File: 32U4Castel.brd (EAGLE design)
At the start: 27.9 x 22.9 mm, 19 parts, among them U1 ATMEGA32U4, Y1 16MHz

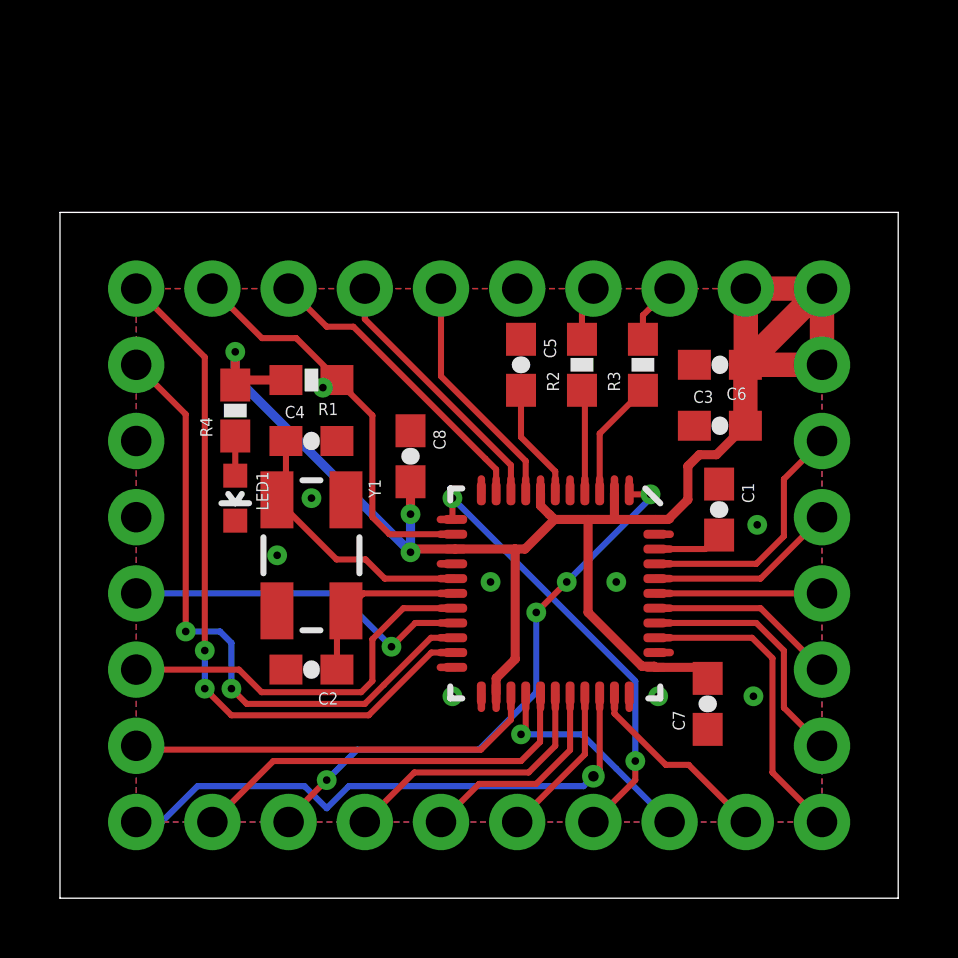
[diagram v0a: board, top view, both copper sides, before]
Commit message: Added pad, complete re-route
Fabrication was difficult because of non-ground vias where 32U4 wanted a pad. Added pad, rerouted everything. Improved silkscreen.
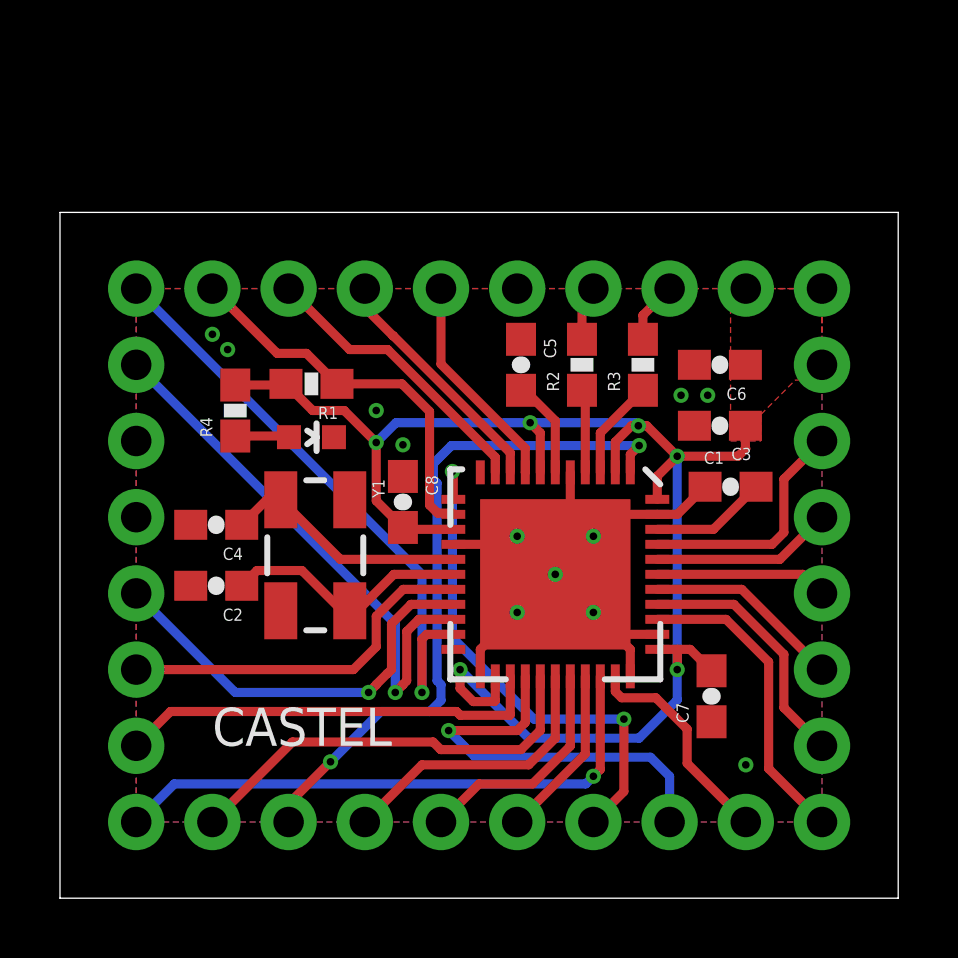
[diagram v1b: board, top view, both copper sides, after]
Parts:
- U1: device Testing:QFN-44-NOPAD_1:1-OUTFAKES -> 32U4Castel:TESTING_QFN-44
- moved C2 4.23 mm to (5.21, 10.4)
- moved C4 4.23 mm to (5.21, 12.4), turned to 180 degrees
- moved LED1 3.25 mm to (8.38, 15.4), turned to 270 degrees
- moved C8 1.55 mm to (11.4, 13.2)
- moved C1 0.85 mm to (22.4, 13.7), turned to 0 degrees
- moved U1 0.63 mm to (16.5, 10.8)
- moved C7 0.28 mm to (21.7, 6.73)
- moved Y1 0.13 mm to (8.51, 11.4)
- moved R1 0.13 mm to (8.38, 17.1)
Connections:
- net GND: now also U1.THERM
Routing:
- net GND: track 0.00 -> 26.7 mm, vias 9 -> 12
- net VCC: track 58.6 -> 52.4 mm, vias 3 -> 6
- net D12: track 7.59 -> 13.7 mm
- net D7: track 19.0 -> 23.2 mm, vias 4 -> 2
- net TXO: track 23.9 -> 20.3 mm, vias 2 -> 1
- net RXI: track 21.4 -> 18.4 mm, vias 2 -> 1
- net D11: track 14.6 -> 17.2 mm
- net N$2: track 5.97 -> 8.32 mm
- net D2: track 11.7 -> 14.1 mm
- net AREF: track 2.32 -> 3.88 mm
- net N$1: track 9.11 -> 8.22 mm
- net D13: track 6.54 -> 7.33 mm
- net D-: track 4.03 -> 3.32 mm
- net MISO: track 7.99 -> 7.29 mm
- net SCK: track 8.84 -> 8.14 mm
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- added copper zone on layer 1, net VCC
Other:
- board text added: "CASTEL"

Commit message: Updated 32U4Castel
Fixed mis-mapped SS pin and improved grounding.
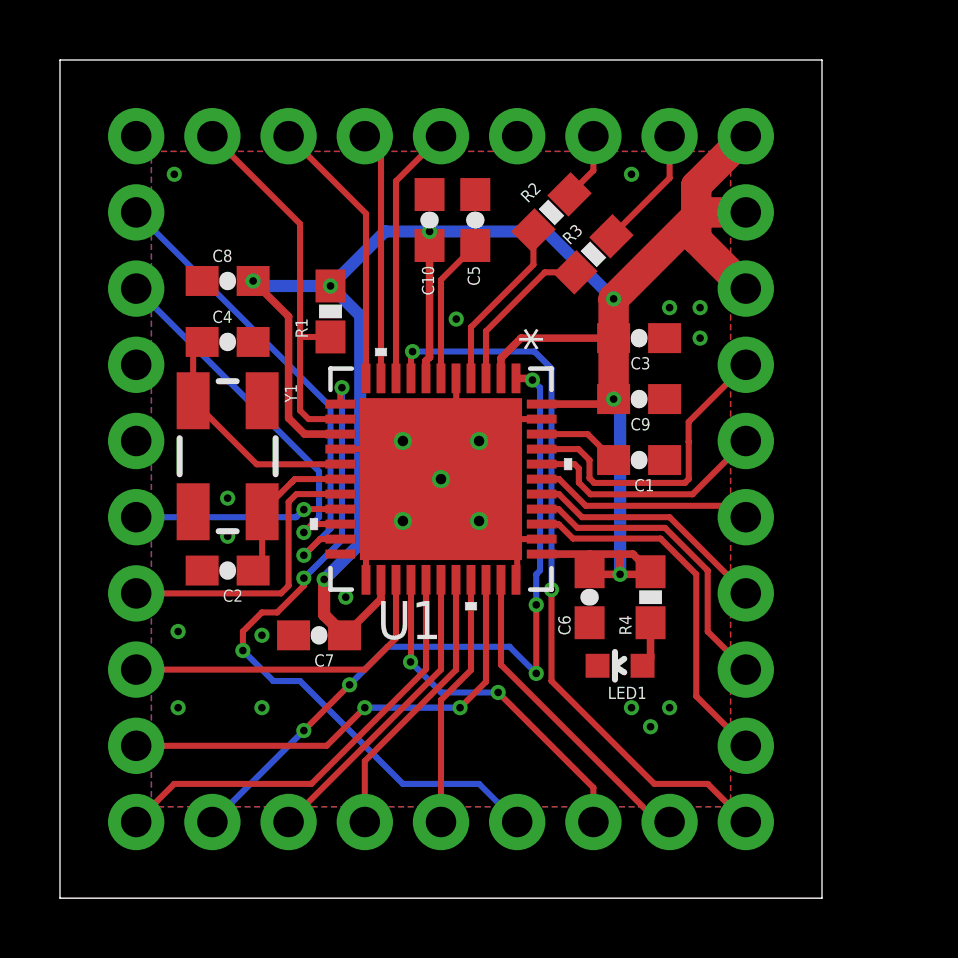
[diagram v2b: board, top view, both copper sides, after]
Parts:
- added C10, C9: 1uF, SparkFun:0603-CAP
- J1, J3: device SparkFun-Connectors:1X08_NO_SILK -> SparkFun-Connectors:1X09_NO_SILK
- U1: value ATMEGA32U4 -> ATMEGA32U4-MU; device 32U4Castel:TESTING_QFN-44 -> 32U4:44PW
- moved J3 22.9 mm to (22.9, 25.4)
- moved J1 17.8 mm to (22.9, 2.54)
- moved R4 15.2 mm to (19.7, 10.0)
- moved C7 13.2 mm to (8.64, 8.76), turned to 0 degrees
- moved LED1 12.8 mm to (18.7, 7.75), turned to 90 degrees
- moved C8 9.40 mm to (5.59, 20.6), turned to 0 degrees
- moved C6 8.88 mm to (17.7, 10.0), turned to 270 degrees
- moved C4 6.11 mm to (5.59, 18.5), turned to 0 degrees
- moved R2 5.18 mm to (16.4, 22.9), turned to 45 degrees
- moved C5 5.06 mm to (13.8, 22.6)
- moved U1 4.96 mm to (12.7, 14.0)
- moved Y1 4.41 mm to (5.59, 14.7)
- moved R3 4.04 mm to (17.8, 21.5), turned to 45 degrees
- moved C3 3.97 mm to (19.3, 18.7), turned to 180 degrees
- moved J4 3.59 mm to (22.9, 5.08)
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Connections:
- net N$1 renamed X2
- net N$2 renamed X1
- net N$38 renamed LED
- net N$4 renamed UCAP
- new net D14: J1.1, U1.8
- net D10: now also J1.5; no longer J3.4
- net D11: now also J1.4; no longer J3.3
- net D12: now also J1.3; no longer J3.2
- net D13: now also J1.2; no longer J3.1
- net D6: now also J1.9; no longer J3.8
- net D7: now also J1.8; no longer J3.7
- net D8: now also J1.7; no longer J3.6
- net D9: now also J1.6; no longer J3.5
- net GND: now also C10.1, C9.1, J3.4, U1.45; no longer J1.4, U1.THERM
- net MISO: now also J3.7, U1.11; no longer J1.5, U1.8
- net MOSI: now also J3.6; no longer J1.7
- net RESET: now also J3.8; no longer J1.8
- net SCK: now also J3.5; no longer J1.6
- net VCC: now also C10.2, C9.2, J3.1; no longer J1.1
- net XD+: now also J3.3; no longer J1.3
- net XD-: now also J3.2; no longer J1.2
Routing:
- net D14: track 0.00 -> 24.6 mm, vias 0 -> 2
- net VCC: track 52.4 -> 76.8 mm, vias 6 -> 7
- net GND: track 26.7 -> 4.99 mm, vias 12 -> 21
- net D2: track 14.1 -> 6.91 mm
- net RXI: track 18.4 -> 12.2 mm
- net D11: track 17.2 -> 22.5 mm, vias 2 -> 3
- net TXO: track 20.3 -> 15.9 mm
- net D5: track 19.3 -> 15.9 mm, vias 1 -> 2
- net D13: track 7.33 -> 10.6 mm
- net D4: track 14.3 -> 11.0 mm
- net X1: track 8.32 -> 5.14 mm
- net D+: track 2.78 -> 5.79 mm
- net D10: track 5.80 -> 8.49 mm
- net D3: track 12.3 -> 9.81 mm
- net A5: track 7.96 -> 10.4 mm
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- removed copper zone on layer 1, net VCC
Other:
- board size 27.9 x 22.9 mm -> 25.4 x 27.9 mm
- board text added: "D10"
- board text added: "D11"
- board text added: "D12"
- board text added: "D13"
- board text added: "D14"
- board text added: "D2"
- board text added: "D3"
- board text added: "D4"
- board text added: "D5"
- board text added: "D6"
- board text added: "D7"
- board text added: "D8"
- board text added: "D9"
- board text added: "Rx"
- board text added: "Tx"
- board text added: "VCC"
- board text removed: "10"
- board text removed: "11"
- board text removed: "12"
- board text removed: "13"
- board text removed: "2"
- board text removed: "3"
- board text removed: "4"
- board text removed: "5"
- board text removed: "5V"
- board text removed: "6"
- board text removed: "7"
- board text removed: "8"
- board text removed: "9"
- board text removed: "CASTEL"
- board text removed: "G"
- board text removed: "RX"
- board text removed: "TX"
